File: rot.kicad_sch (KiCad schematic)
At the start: 35 parts

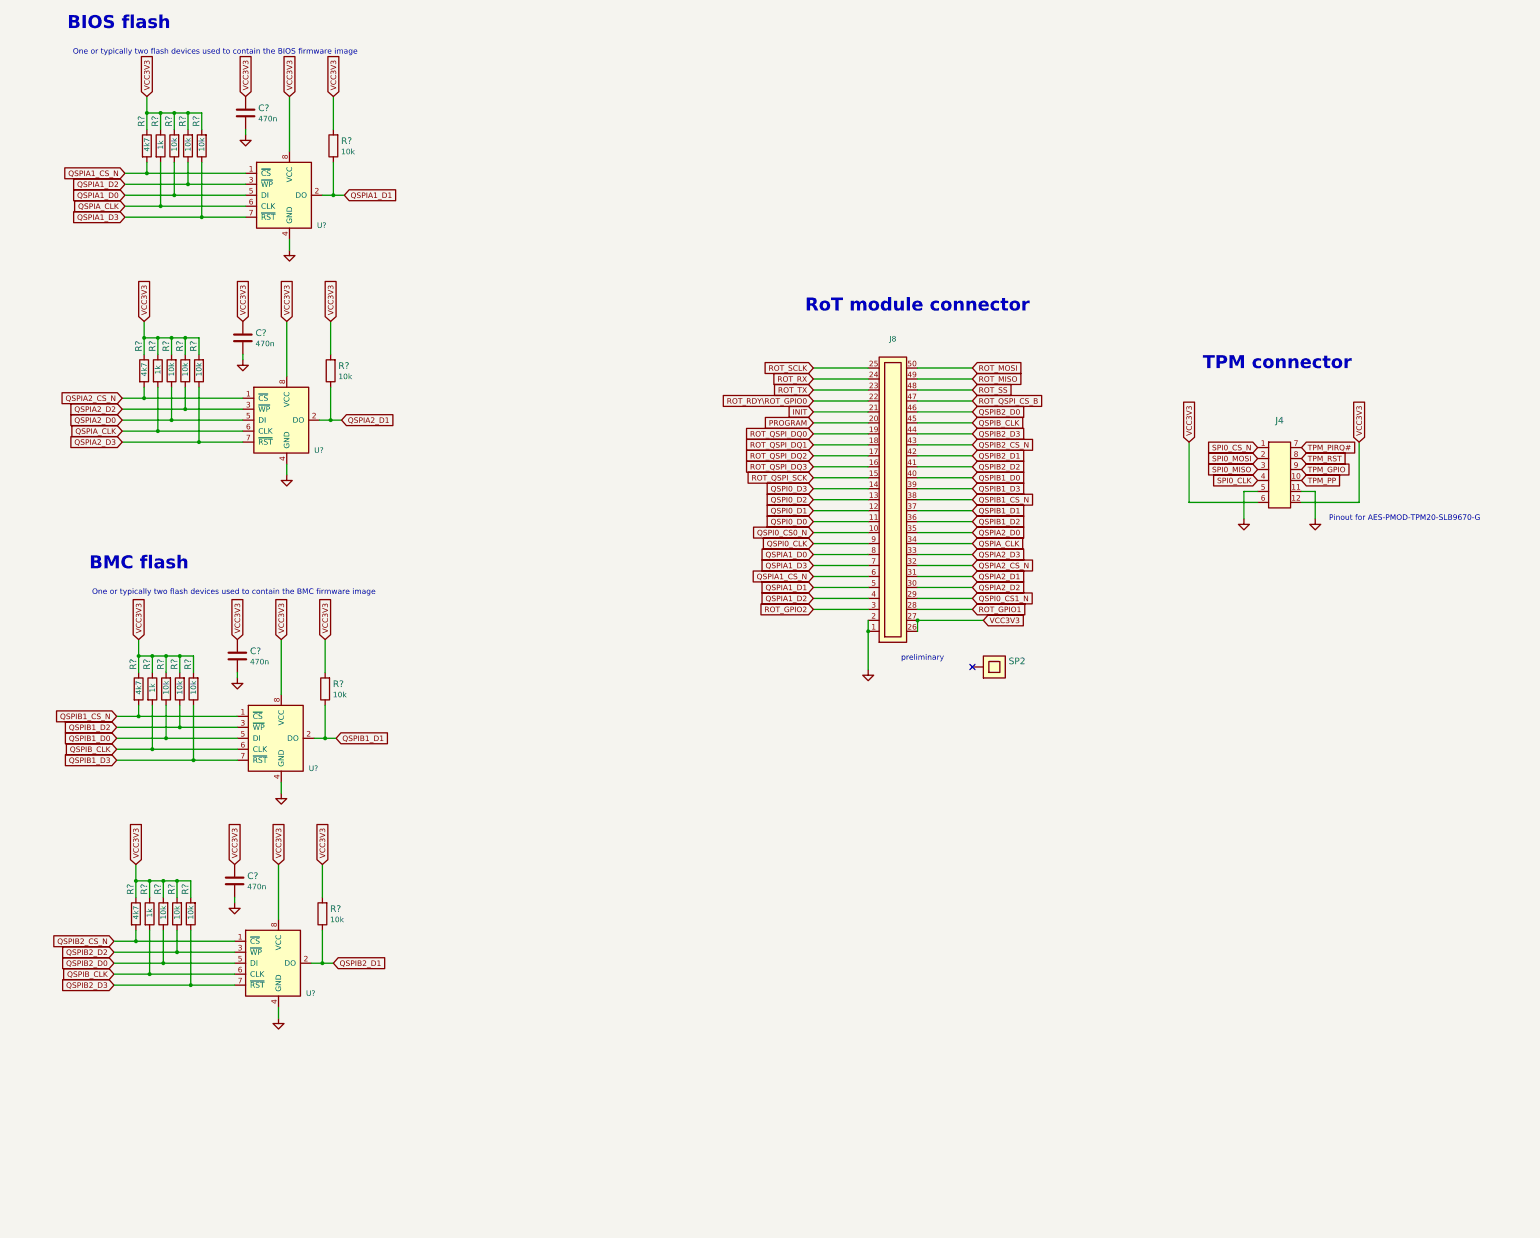
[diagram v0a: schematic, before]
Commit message: Introduce component standardization
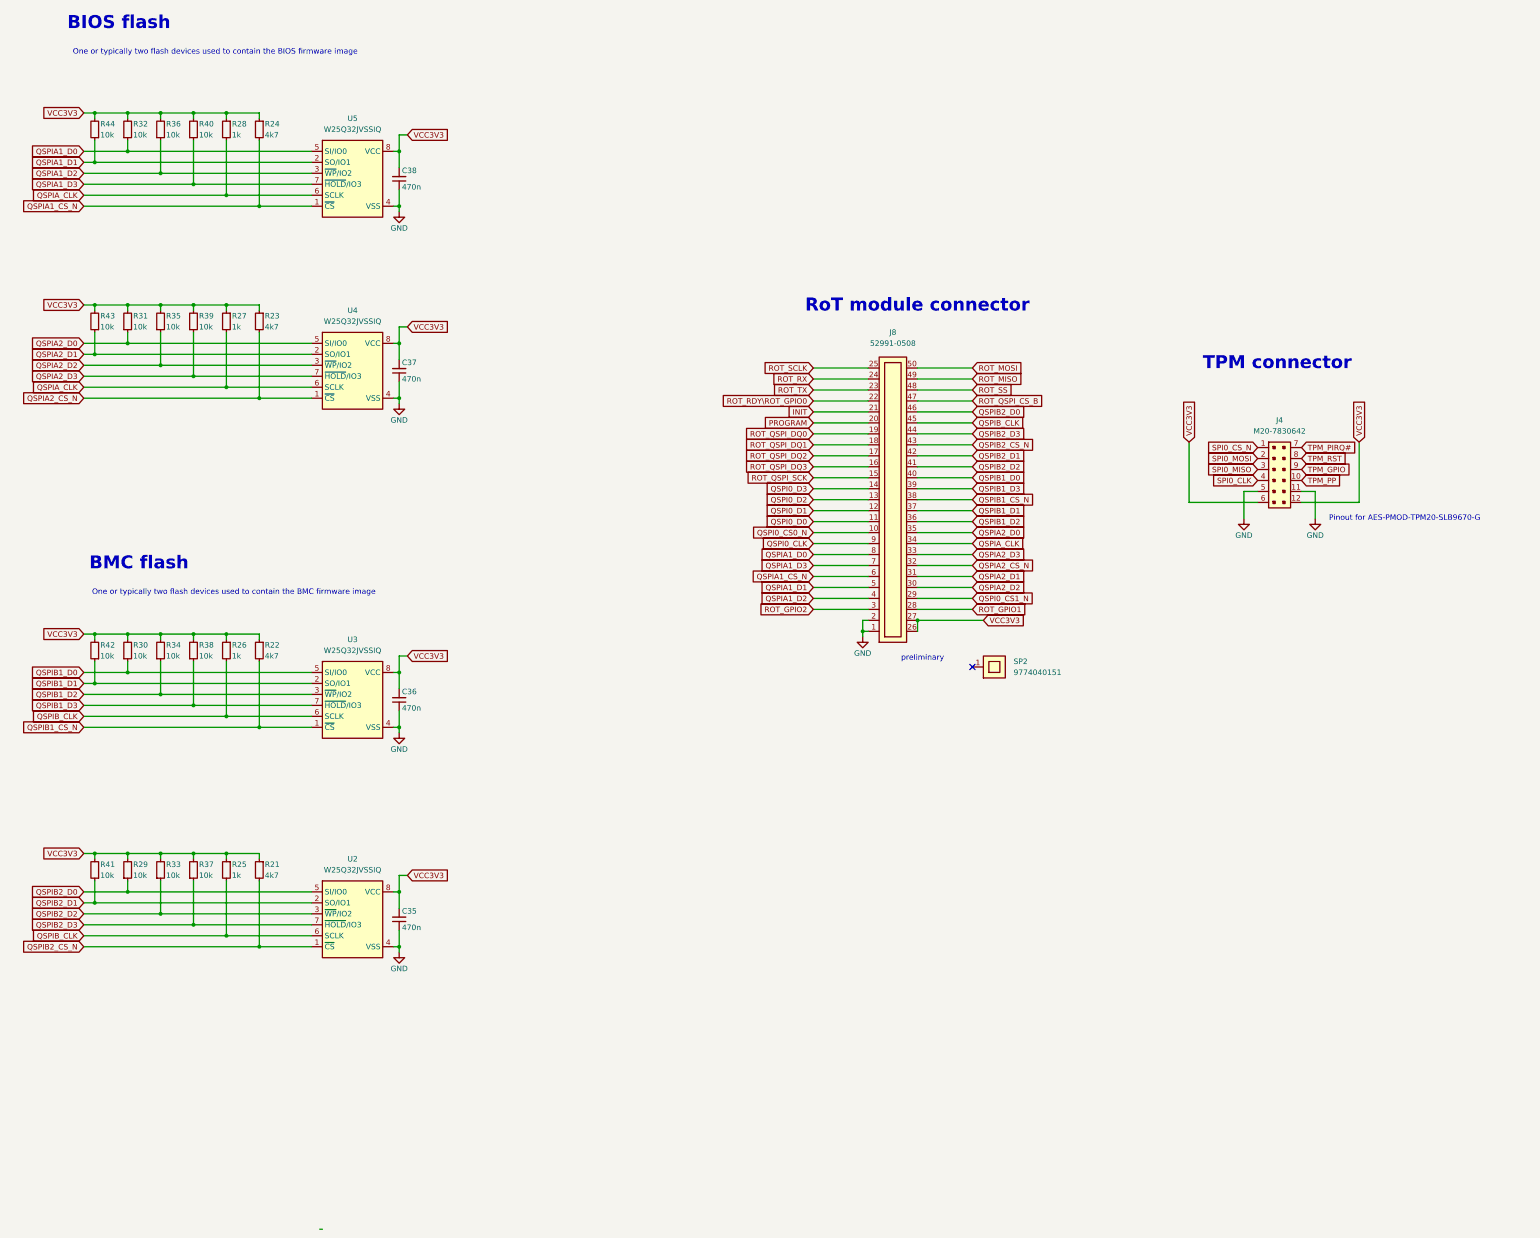
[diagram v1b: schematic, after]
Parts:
- C35, C36, C37, C38: renamed from C?; value (none) -> C_470n_0402; footprint (none) -> antmicro-footprints:C_0402_1005Metric; symbol artix-dc-scm:C_470n_0402 -> antmicroCapacitors0402:C_470n_0402; Author (none) -> Antmicro; License (none) -> Apache-2.0
- J4: value (none) -> PinSocket_6x2_P2.54mm; footprint (none) -> antmicro-footprints:PinHeader_6x2_P2.54mm_Vertical_pmod; symbol artix-dc-scm:M20-7830642 -> antmicroRectangularConnectorsHeadersFemalePins:PinSocket_6x2_P2.54mm; Author (none) -> Antmicro; License (none) -> Apache-2.0; Manufacturer Molex -> Harwin
- J8: value (none) -> Molex_SlimStack_2x25_P0.5mm_529910-508; footprint (none) -> antmicro-footprints:Conn_Molex_SlimStack_529910-508_2x25_P0.5mm; symbol artix-dc-scm:52991-0508 -> antmicroB2bConnectors:Molex_SlimStack_2x25_P0.5mm_529910-508; Author (none) -> Antmicro; License (none) -> Apache-2.0; MPN (none) -> 52991-0508; Manufacturer (none) -> Molex
- R21, R22, R23, R24: renamed from R?; value (none) -> R_4k7_0402; footprint (none) -> antmicro-footprints:R_0402_1005Metric; symbol artix-dc-scm:R_4k7_0402 -> antmicroResistors0402:R_4k7_0402; Author (none) -> Antmicro; License (none) -> Apache-2.0; MPN ERJ2GEJ472X -> CR0402-FX-4701GLF; Manufacturer PANASONIC_ELECTRONIC_COMPONENTS -> Bourns; Tolerance (none) -> 1%
- R25, R26, R27, R28: renamed from R?; value (none) -> R_1k_0402; footprint (none) -> antmicro-footprints:R_0402_1005Metric; symbol artix-dc-scm:R_1k_0402 -> antmicroResistors0402:R_1k_0402; Author (none) -> Antmicro; License (none) -> Apache-2.0; Manufacturer BOURNS -> Bourns; Tolerance (none) -> 1%
- R29, R30, R31, R32, R33, R34, R35, R36, R37, R38, R39, R40, R41, R42, R43, R44: renamed from R?; value (none) -> R_10k_0402; footprint (none) -> antmicro-footprints:R_0402_1005Metric; symbol artix-dc-scm:R_10k_0402 -> antmicroResistors0402:R_10k_0402; Author (none) -> Antmicro; License (none) -> Apache-2.0; MPN CRCW040210K0FKEDHP -> CR0402-FX-1002GLF; Manufacturer VISHAY -> Bourns; Tolerance (none) -> 1%
- SP2: value (none) -> 9774040151; footprint (none) -> antmicro-footprints:9774040151; symbol artix-dc-scm:9774040151 -> antmicroMechanicalParts:9774040151; Author (none) -> Antmicro; License (none) -> Apache-2.0; MPN 9774030151 -> 9774040151R; Manufacturer Wurth Elektronik -> Würth Elektronik
- U2, U3, U4, U5: renamed from U?; value (none) -> W25Q32JV_SOIC-8; footprint (none) -> antmicro-footprints:SOIC-8-1EP_5.3x5.3x2mm_P1.27mm; symbol artix-dc-scm:W25Q32JVSSIQ_TR -> antmicroMemory:W25Q32JV_SOIC-8; Author (none) -> Antmicro; License (none) -> Apache-2.0; MPN W25Q32JVSSIQ TR -> W25Q32JVSSIQ; Manufacturer Winbond Electronics -> GigaDevice
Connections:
- net GND: now also C35.1, C36.1, C37.1, C38.1; no longer C35.2, C36.2, C37.2, C38.2
- net VCC3V3: now also C35.2, C36.2, C37.2, C38.2; no longer C35.1, C36.1, C37.1, C38.1
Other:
- moved on the sheet: C35, C36, C37, C38, R21, R22, R23, R24, R25, R26, R27, R28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

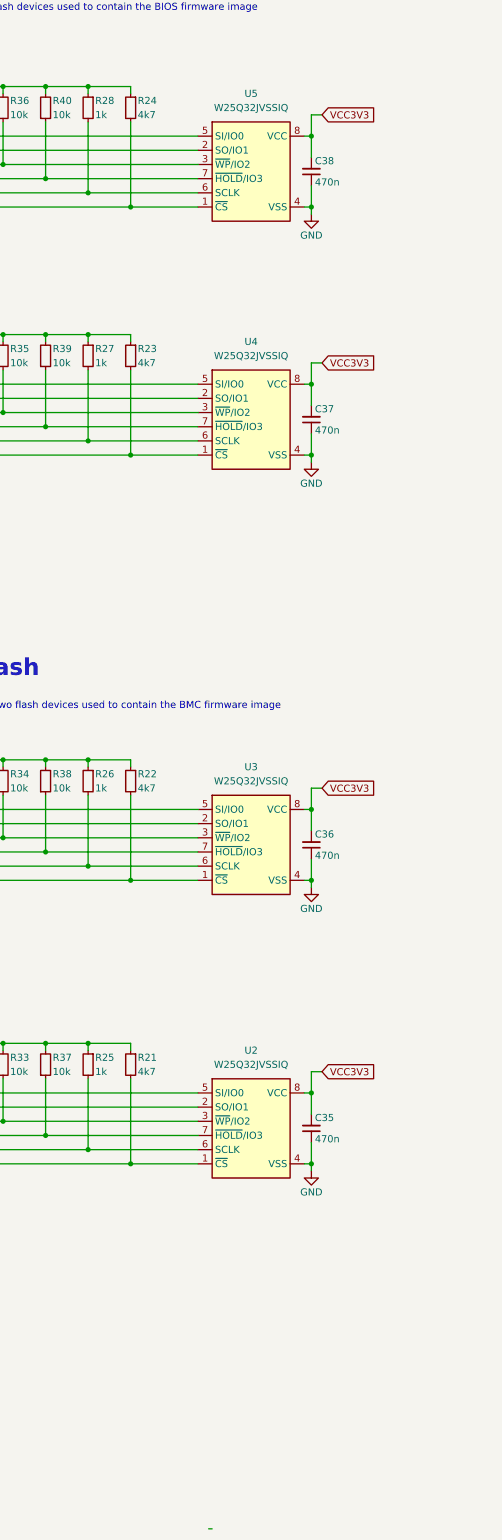
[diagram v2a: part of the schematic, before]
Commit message: Fix schematic ERC errors. ERC clean
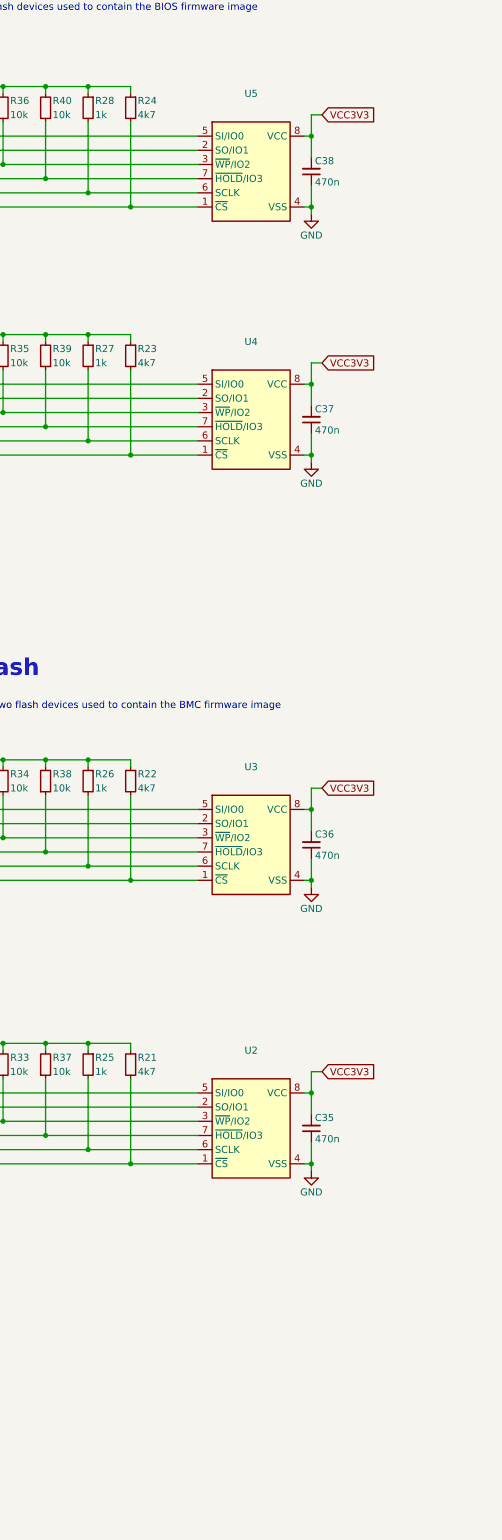
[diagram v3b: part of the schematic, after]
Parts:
- U2, U3, U4, U5: symbol antmicroMemory:W25Q32JV_SOIC-8 -> antmicroMemory:W25Q32JW_SOIC-8; MPN W25Q32JVSSIQ -> W25Q32JWSSIQ; Manufacturer GigaDevice -> Winbond
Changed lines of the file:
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@@
-    (stroke (width 0) (type default) (color 0 0 0 0))
-  )
-  (wire (pts (xy 94.615 309.245) (xy 95.25 309.245))
     (stroke (width 0) (type default) (color 0 0 0 0))
   )
@@
     (pin "2")
   )
-  (symbol (lib_id "antmicroMemory:W25Q32JV_SOIC-8") (at 92.71 59.69 0) (unit 1)
+  (symbol (lib_id "antmicroMemory:W25Q32JW_SOIC-8") (at 92.71 59.69 0) (unit 1)
     (in_bom yes) (on_board yes) (fields_autoplaced)
     (property "Reference" "U5" (id 0) (at 102.235 52.07 0))
@@
       (effects (font (size 1.27 1.27) (thickness 0.15)) (justify left bottom) hide)
     )
-    (property "Datasheet" "https://www.mouser.pl/datasheet/2/949/w25q32jv_revg_03272018_plus-1489806.pdf" (id 3) (at 125.73 71.12 0)
-      (effects (font (size 1.27 1.27) (thickness 0.15)) (justify left bottom) hide)
-    )
-    (property "MPN" "W25Q32JVSSIQ" (id 4) (at 102.235 54.61 0)
-      (effects (font (size 1.27 1.27) (thickness 0.15)))
-    )
-    (property "Manufacturer" "GigaDevice" (id 5) (at 125.73 76.2 0)
+    (property "Datasheet" "https://www.mouser.pl/datasheet/2/949/w25q32jw_spi_revf_09042018-1489621.pdf" (id 3) (at 125.73 71.12 0)
+      (effects (font (size 1.27 1.27) (thickness 0.15)) (justify left bottom) hide)
+    )
+    (property "MPN" "W25Q32JWSSIQ" (id 4) (at 125.73 73.66 0)
+      (effects (font (size 1.27 1.27) (thickness 0.15)) (justify left bottom) hide)
+    )
+    (property "Manufacturer" "Winbond" (id 5) (at 125.73 76.2 0)
       (effects (font (size 1.27 1.27) (thickness 0.15)) (justify left bottom) hide)
     )
@@
       (effects (font (size 1.27 1.27)) hide)
     )
+    (property "Author" "Antmicro" (id 4) (at 317.5 152.4 0)
+      (effects (font (size 1.27 1.27) (thickness 0.15)) (justify left bottom) hide)
+    )
+    (property "License" "Apache-2.0" (id 5) (at 317.5 154.94 0)
+      (effects (font (size 1.27 1.27) (thickness 0.15)) (justify left bottom) hide)
+    )
     (pin "1")
   )
@@
       (effects (font (size 1.27 1.27)) hide)
     )
+    (property "Author" "Antmicro" (id 4) (at 334.01 152.4 0)
+      (effects (font (size 1.27 1.27) (thickness 0.15)) (justify left bottom) hide)
+    )
+    (property "License" "Apache-2.0" (id 5) (at 334.01 154.94 0)
+      (effects (font (size 1.27 1.27) (thickness 0.15)) (justify left bottom) hide)
+    )
     (pin "1")
   )
@@
     (pin "2")
   )
-  (symbol (lib_id "antmicroMemory:W25Q32JV_SOIC-8") (at 92.71 104.14 0) (unit 1)
+  (symbol (lib_id "antmicroMemory:W25Q32JW_SOIC-8") (at 92.71 104.14 0) (unit 1)
     (in_bom yes) (on_board yes) (fields_autoplaced)
     (property "Reference" "U4" (id 0) (at 102.235 96.52 0))
@@
       (effects (font (size 1.27 1.27) (thickness 0.15)) (justify left bottom) hide)
     )
-    (property "Datasheet" "https://www.mouser.pl/datasheet/2/949/w25q32jv_revg_03272018_plus-1489806.pdf" (id 3) (at 125.73 115.57 0)
-      (effects (font (size 1.27 1.27) (thickness 0.15)) (justify left bottom) hide)
-    )
-    (property "MPN" "W25Q32JVSSIQ" (id 4) (at 102.235 99.06 0)
-      (effects (font (size 1.27 1.27) (thickness 0.15)))
-    )
-    (property "Manufacturer" "GigaDevice" (id 5) (at 125.73 120.65 0)
+    (property "Datasheet" "https://www.mouser.pl/datasheet/2/949/w25q32jw_spi_revf_09042018-1489621.pdf" (id 3) (at 125.73 115.57 0)
+      (effects (font (size 1.27 1.27) (thickness 0.15)) (justify left bottom) hide)
+    )
+    (property "MPN" "W25Q32JWSSIQ" (id 4) (at 125.73 118.11 0)
+      (effects (font (size 1.27 1.27) (thickness 0.15)) (justify left bottom) hide)
+    )
+    (property "Manufacturer" "Winbond" (id 5) (at 125.73 120.65 0)
       (effects (font (size 1.27 1.27) (thickness 0.15)) (justify left bottom) hide)
     )
@@
     (pin "2")
   )
-  (symbol (lib_id "antmicroMemory:W25Q32JV_SOIC-8") (at 92.71 180.34 0) (unit 1)
+  (symbol (lib_id "antmicroMemory:W25Q32JW_SOIC-8") (at 92.71 180.34 0) (unit 1)
     (in_bom yes) (on_board yes) (fields_autoplaced)
     (property "Reference" "U3" (id 0) (at 102.235 172.72 0))
@@
       (effects (font (size 1.27 1.27) (thickness 0.15)) (justify left bottom) hide)
     )
-    (property "Datasheet" "https://www.mouser.pl/datasheet/2/949/w25q32jv_revg_03272018_plus-1489806.pdf" (id 3) (at 125.73 191.77 0)
-      (effects (font (size 1.27 1.27) (thickness 0.15)) (justify left bottom) hide)
-    )
-    (property "MPN" "W25Q32JVSSIQ" (id 4) (at 102.235 175.26 0)
-      (effects (font (size 1.27 1.27) (thickness 0.15)))
-    )
-    (property "Manufacturer" "GigaDevice" (id 5) (at 125.73 196.85 0)
+    (property "Datasheet" "https://www.mouser.pl/datasheet/2/949/w25q32jw_spi_revf_09042018-1489621.pdf" (id 3) (at 125.73 191.77 0)
+      (effects (font (size 1.27 1.27) (thickness 0.15)) (justify left bottom) hide)
+    )
+    (property "MPN" "W25Q32JWSSIQ" (id 4) (at 125.73 194.31 0)
+      (effects (font (size 1.27 1.27) (thickness 0.15)) (justify left bottom) hide)
+    )
+    (property "Manufacturer" "Winbond" (id 5) (at 125.73 196.85 0)
       (effects (font (size 1.27 1.27) (thickness 0.15)) (justify left bottom) hide)
     )
@@
     (pin "2")
   )
-  (symbol (lib_id "antmicroMemory:W25Q32JV_SOIC-8") (at 92.71 231.14 0) (unit 1)
+  (symbol (lib_id "antmicroMemory:W25Q32JW_SOIC-8") (at 92.71 231.14 0) (unit 1)
     (in_bom yes) (on_board yes) (fields_autoplaced)
     (property "Reference" "U2" (id 0) (at 102.235 223.52 0))
@@
       (effects (font (size 1.27 1.27) (thickness 0.15)) (justify left bottom) hide)
     )
-    (property "Datasheet" "https://www.mouser.pl/datasheet/2/949/w25q32jv_revg_03272018_plus-1489806.pdf" (id 3) (at 125.73 242.57 0)
-      (effects (font (size 1.27 1.27) (thickness 0.15)) (justify left bottom) hide)
-    )
-    (property "MPN" "W25Q32JVSSIQ" (id 4) (at 102.235 226.06 0)
-      (effects (font (size 1.27 1.27) (thickness 0.15)))
-    )
-    (property "Manufacturer" "GigaDevice" (id 5) (at 125.73 247.65 0)
+    (property "Datasheet" "https://www.mouser.pl/datasheet/2/949/w25q32jw_spi_revf_09042018-1489621.pdf" (id 3) (at 125.73 242.57 0)
+      (effects (font (size 1.27 1.27) (thickness 0.15)) (justify left bottom) hide)
+    )
+    (property "MPN" "W25Q32JWSSIQ" (id 4) (at 125.73 245.11 0)
+      (effects (font (size 1.27 1.27) (thickness 0.15)) (justify left bottom) hide)
+    )
+    (property "Manufacturer" "Winbond" (id 5) (at 125.73 247.65 0)
       (effects (font (size 1.27 1.27) (thickness 0.15)) (justify left bottom) hide)
     )
@@
       (effects (font (size 1.27 1.27)) hide)
     )
+    (property "Author" "Antmicro" (id 4) (at 211.455 179.705 0)
+      (effects (font (size 1.27 1.27) (thickness 0.15)) (justify left bottom) hide)
+    )
+    (property "License" "Apache-2.0" (id 5) (at 211.455 182.245 0)
+      (effects (font (size 1.27 1.27) (thickness 0.15)) (justify left bottom) hide)
+    )
     (pin "1")
   )
@@
       (effects (font (size 1.27 1.27)) hide)
     )
+    (property "Author" "Antmicro" (id 4) (at 104.14 125.73 0)
+      (effects (font (size 1.27 1.27) (thickness 0.15)) (justify left bottom) hide)
+    )
+    (property "License" "Apache-2.0" (id 5) (at 104.14 128.27 0)
+      (effects (font (size 1.27 1.27) (thickness 0.15)) (justify left bottom) hide)
+    )
     (pin "1")
   )
@@
       (effects (font (size 1.27 1.27)) hide)
     )
+    (property "Author" "Antmicro" (id 4) (at 104.14 252.73 0)
+      (effects (font (size 1.27 1.27) (thickness 0.15)) (justify left bottom) hide)
+    )
+    (property "License" "Apache-2.0" (id 5) (at 104.14 255.27 0)
+      (effects (font (size 1.27 1.27) (thickness 0.15)) (justify left bottom) hide)
+    )
     (pin "1")
   )
@@
       (effects (font (size 1.27 1.27)) hide)
     )
+    (property "Author" "Antmicro" (id 4) (at 104.14 201.93 0)
+      (effects (font (size 1.27 1.27) (thickness 0.15)) (justify left bottom) hide)
+    )
+    (property "License" "Apache-2.0" (id 5) (at 104.14 204.47 0)
+      (effects (font (size 1.27 1.27) (thickness 0.15)) (justify left bottom) hide)
+    )
     (pin "1")
   )
@@
       (effects (font (size 1.27 1.27)) hide)
     )
-    (pin "1")
+    (property "Author" "Antmicro" (id 4) (at 104.14 81.28 0)
+      (effects (font (size 1.27 1.27) (thickness 0.15)) (justify left bottom) hide)
+    )
+    (property "License" "Apache-2.0" (id 5) (at 104.14 83.82 0)
+      (effects (font (size 1.27 1.27) (thickness 0.15)) (justify left bottom) hide)
+    )
+    (pin "1")
